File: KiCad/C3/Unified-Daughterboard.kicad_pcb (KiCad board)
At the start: 2 copper layers, 18 x 16.5 mm, 14 parts, among them J1 TYPE-C-31-M12_13, J2 SM04B-SRSS-TB(LF)(SN), U1 TPD4E05U06DQAR

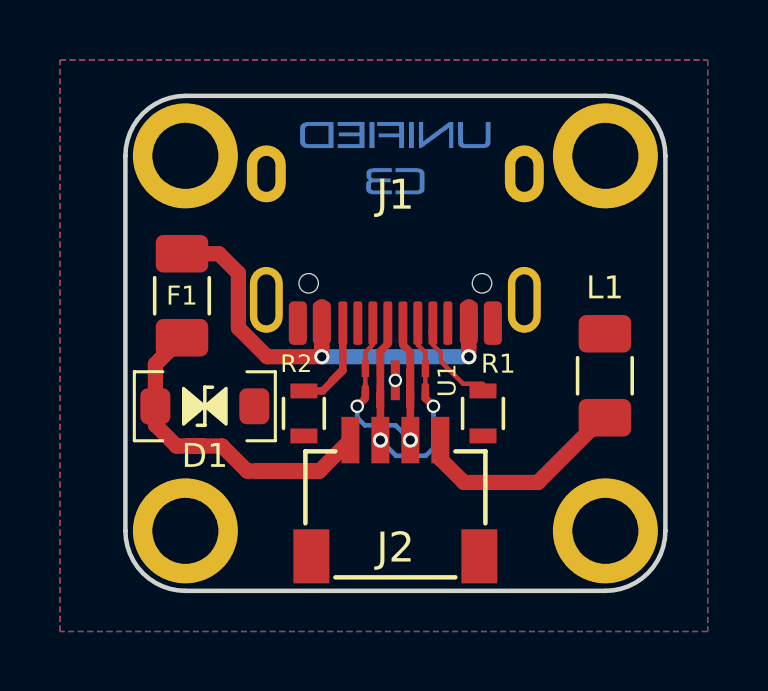
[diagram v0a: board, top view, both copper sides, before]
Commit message: Make version with JLCPCB tooling holes and ID number
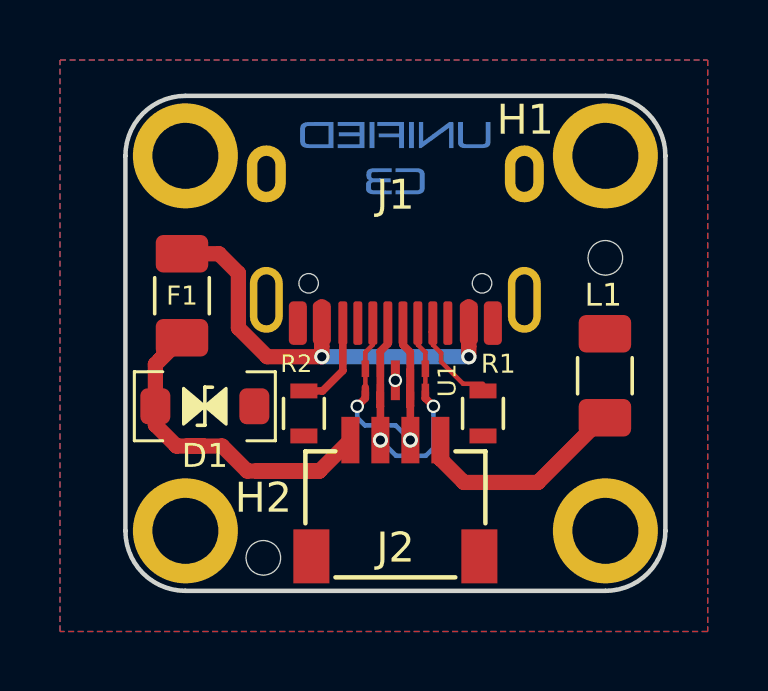
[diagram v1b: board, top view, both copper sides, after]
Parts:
- added H1: JLCPCB Tooling Hole, acheron_MountingHoles:ToolingHole_1.152mm_(for_JLCPCB_SMT), F.Cu at (82.0, 61.9)
- added H2: JLCPCB Tooling Hole, acheron_MountingHoles:ToolingHole_1.152mm_(for_JLCPCB_SMT), F.Cu at (70.6, 71.9)
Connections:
- J1 pad A8: Net-(J1-PadA8) -> unconnected-(J1-PadA8)
- J1 pad B8: Net-(J1-PadB8) -> unconnected-(J1-PadB8)
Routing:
- net DA-: track 13.4 -> 12.1 mm
- net Net-(J1-PadB5): track 6.33 -> 5.74 mm
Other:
- net class Default removed
- net class Power removed
- board text added: "JLCJLCJLCJLC"
